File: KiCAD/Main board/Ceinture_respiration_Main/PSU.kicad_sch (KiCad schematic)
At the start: 8 parts, among them J11 Conn_01x02, Q2 AP10N04S

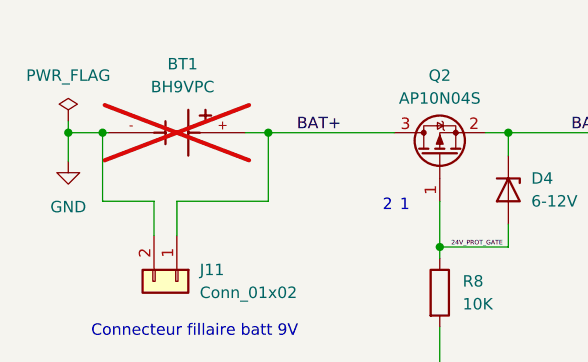
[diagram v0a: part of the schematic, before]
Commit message: modifié info Part number du main board pour faciliter la génération de BOM non JLC
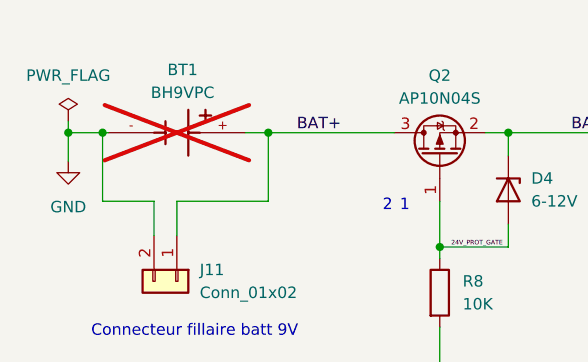
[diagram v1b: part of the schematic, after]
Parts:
- BT1: MPN (none) -> BH9VPC or 36-233-ND
- D5: LCSC (none) -> C2895472
- S1: MPN (none) -> EG1218
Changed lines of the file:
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@@
+			)
+		)
+		(property "MPN" "EG1218"
+			(at 134.62 45.085 90)
+			(effects
+				(font
+					(size 1.27 1.27)
+				)
+				(hide yes)
 			)
 		)
@@
 			)
 		)
+		(property "LCSC" "C2895472"
+			(at 157.48 72.0725 0)
+			(effects
+				(font
+					(size 1.27 1.27)
+				)
+				(hide yes)
+			)
+		)
 		(pin "1"
 		)
@@
 		(fields_autoplaced yes)
 		(property "Reference" "BT1"
-			(at 67.945 40.005 0)
+			(at 67.945 40.64 0)
 			(effects
 				(font
@@
 		)
 		(property "Value" "BH9VPC"
-			(at 67.945 42.545 0)
+			(at 67.945 43.18 0)
 			(effects
 				(font
@@
 				(hide yes)
 			)
+		)
+		(property "MPN" "BH9VPC or 36-233-ND"
+			(at 67.31 47.625 0)
+			(effects
+				(font
+					(size 1.27 1.27)
+				)
+				(hide yes)
+			)
